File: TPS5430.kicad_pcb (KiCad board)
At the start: 2 copper layers, 55 x 20 mm, 44 parts, among them J1 Barrel_Jack, J2 Screw_Terminal_01x02, Q1 AO3401A, Q2 MMBT3904, U1 TPS5430DDA

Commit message: Finished variable feedback block
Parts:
- added JP5: SolderJumper, Jumper:SolderJumper-2_P1.3mm_Open_RoundedPad1.0x1.5mm, F.Cu at (160.2, 84.5)
- added R12: 390, Resistor_SMD:R_0603_1608Metric, F.Cu at (160.0, 87.5)
- added RV1: 1k, Potentiometer_THT:Potentiometer_Bourns_3296W_Vertical, F.Cu at (160.2, 93.0)
- added RV2: 10k, Potentiometer_THT:Potentiometer_Bourns_3296W_Vertical, F.Cu at (161.5, 79.0)
- J1: value Barrel_Jack -> Screw_Terminal_01x02; footprint tps5430:DC-005-5A-2.0-SMT -> TerminalBlock_Phoenix:TerminalBlock_Phoenix_PT-1,5-2-3.5-H_1x02_P3.50mm_Horizontal
- moved J1 2.51 mm to (152.5, 84.2), turned to -90 degrees
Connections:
- net Net-(F1-Pad1) renamed VDC

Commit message: Completed placement and routing; Updated REAMME and docs
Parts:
- added Logo: LOGO, footprints:Orens_Lab_Logo_5x5mm.kicad_sym, F.Cu at (166.9, 81.7)
- moved LOGO1 13.1 mm to (167.4, 89.4), turned to -90 degrees
- moved JP5 9.29 mm to (166.2, 77.5)
- moved RV1 8.16 mm to (159.6, 84.9), turned to 90 degrees
- moved R12 5.09 mm to (163.6, 83.8), turned to 90 degrees
- moved JP4 0.75 mm to (169.4, 79.3)
- moved JP3 0.55 mm to (172.8, 79.3)
- moved F1 0.45 mm to (166.2, 81.3)
- moved JP2 0.30 mm to (176.0, 79.3)
- moved J1 0.21 mm to (152.7, 84.4)
- renumbered JP3 to JP1, JP1 to JP3
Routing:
- net Net-(RV1-Pad1): track 0.00 -> 21.0 mm
- net VDC: track 0.00 -> 15.3 mm
- net Net-(R12-Pad1): track 0.00 -> 5.08 mm
- net Net-(JP5-A): track 0.00 -> 4.45 mm
- net /Feedback: track 35.7 -> 39.0 mm
- net GND: vias 113 -> 94
- removed copper zone on F.Cu, net VDC
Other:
- board text added: "06/2025"
- board text added: "COURSE^ADJ"
- board text added: "FINE^ADJ"
- board text added: "Input: 5.5-36v"
- board text added: "Oren's Lab"
- board text added: "Rev. 0.1"
- board text added: "VAR"
- board text added: "Vin+"
- board text added: "Vin-"
- board text added: "Vout+"
- board text added: "Vout-"
- board text removed: "07/2021"
- board text removed: "Max Stabel"
- board text removed: "Rev. 1.1"
- board text removed: "git.io/JWgnY"

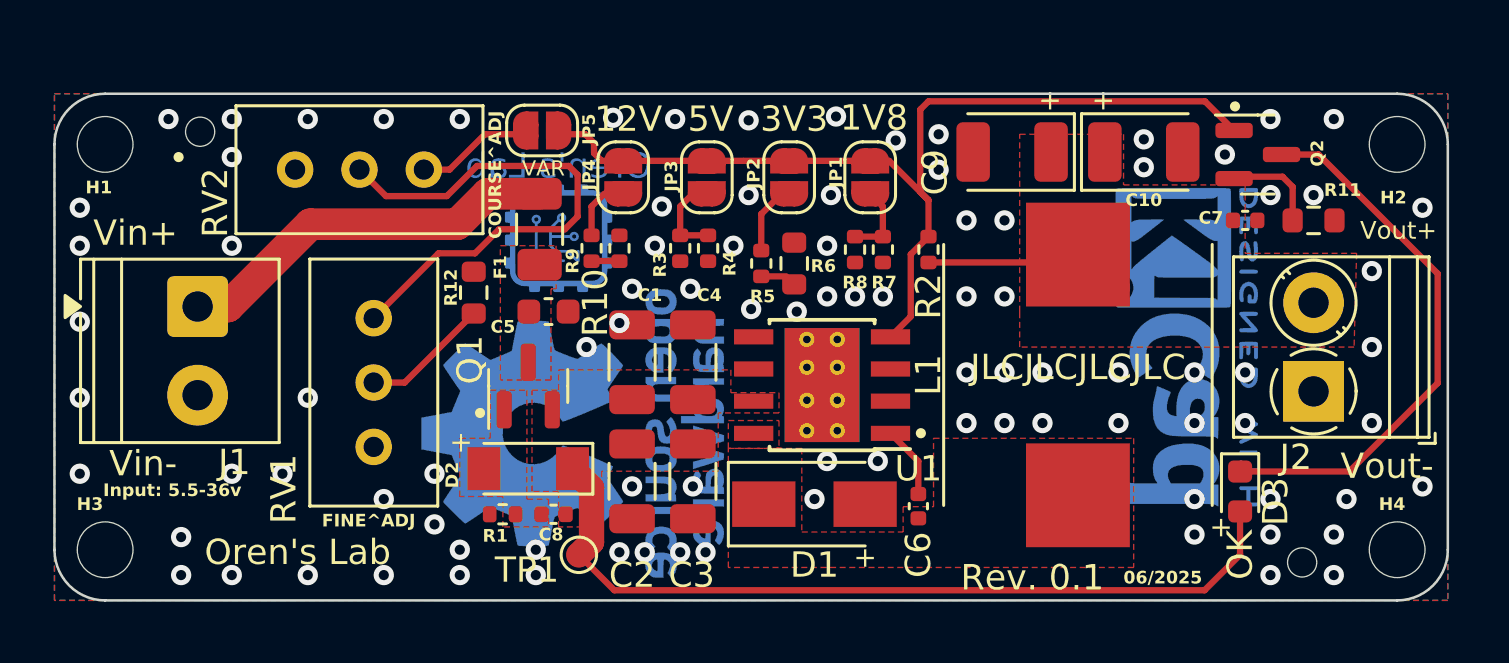
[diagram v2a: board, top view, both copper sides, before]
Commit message: printed PCB updates
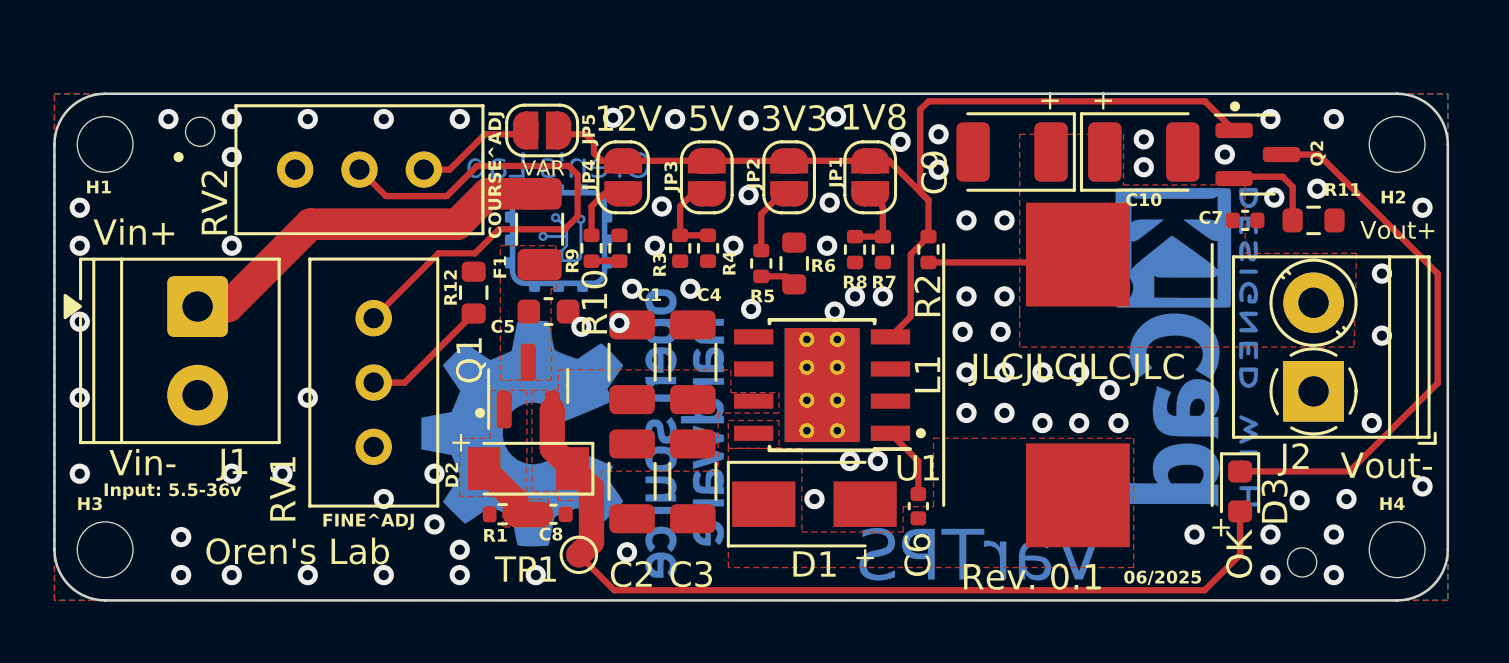
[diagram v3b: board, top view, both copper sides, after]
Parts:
- moved Logo 0.17 mm to (166.7, 81.7)
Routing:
- net Net-(D2-A): track 0.00 -> 3.32 mm
- net VCC: track 32.9 -> 35.5 mm
- net GND: vias 94 -> 86
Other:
- board text added: "VarTPS"
